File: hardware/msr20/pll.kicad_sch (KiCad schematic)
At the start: 9 parts, among them U6 74LS163, U7 CD74HC4046

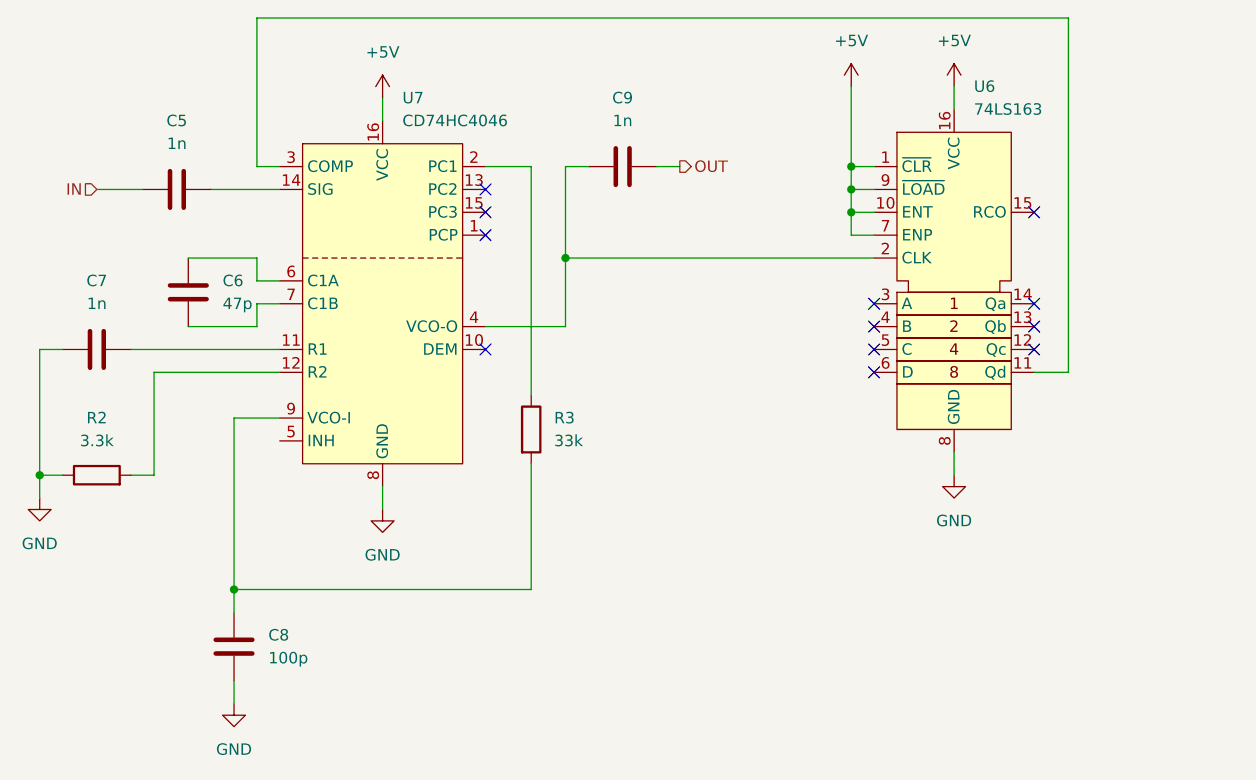
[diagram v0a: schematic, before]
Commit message: add test points to schematic
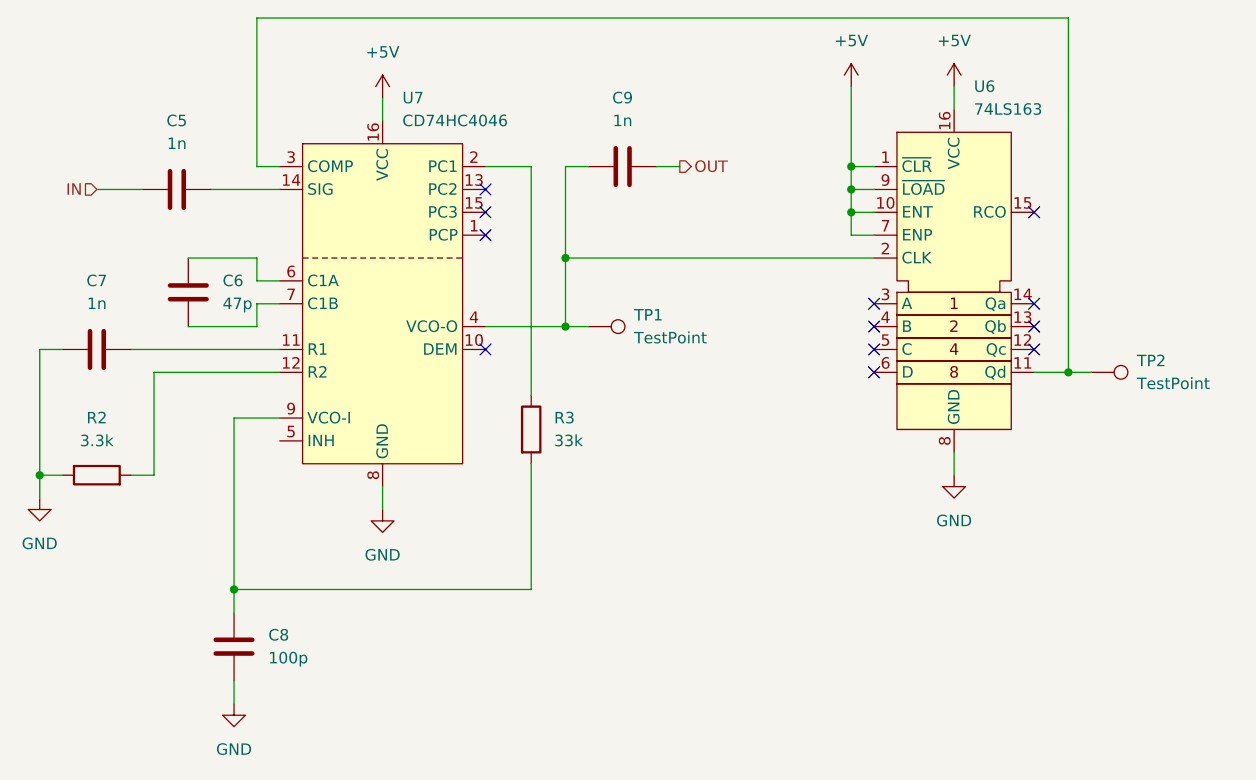
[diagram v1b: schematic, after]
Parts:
- added TP1, TP2: TestPoint, TestPoint:TestPoint_Pad_D1.0mm, symbol Connector:TestPoint
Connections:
- net at U6.11 (Qd), U7.3 (COMP): now also TP2.1
- net at C9.1, U6.2 (CLK), U7.4 (VCO-O): now also TP1.1
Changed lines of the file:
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@@
+		(color 0 0 0 0)
+	)
+	(junction
+		(at 121.92 93.98)
+		(diameter 0)
+		(color 0 0 0 0)
+	)
+	(junction
+		(at 177.8 99.06)
+		(diameter 0)
 		(color 0 0 0 0)
 	)
@@
 	(wire
 		(pts
+			(xy 121.92 93.98) (xy 124.46 93.98)
+		)
+		(stroke
+			(width 0)
+			(type default)
+		)
+	)
+	(wire
+		(pts
 			(xy 121.92 86.36) (xy 156.21 86.36)
 		)
@@
 		(pts
 			(xy 85.09 123.19) (xy 85.09 125.73)
+		)
+		(stroke
+			(width 0)
+			(type default)
+		)
+	)
+	(wire
+		(pts
+			(xy 177.8 99.06) (xy 180.34 99.06)
 		)
 		(stroke
@@
 	)
 	(symbol
+		(lib_id "Connector:TestPoint")
+		(at 180.34 99.06 270)
+		(unit 1)
+		(exclude_from_sim no)
+		(in_bom yes)
+		(on_board yes)
+		(dnp no)
+		(fields_autoplaced yes)
+		(property "Reference" "TP2"
+			(at 185.42 97.7899 90)
+			(effects
+				(font
+					(size 1.27 1.27)
+				)
+				(justify left)
+			)
+		)
+		(property "Value" "TestPoint"
+			(at 185.42 100.3299 90)
+			(effects
+				(font
+					(size 1.27 1.27)
+				)
+				(justify left)
+			)
+		)
+		(property "Footprint" "TestPoint:TestPoint_Pad_D1.0mm"
+			(at 180.34 104.14 0)
+			(effects
+				(font
+					(size 1.27 1.27)
+				)
+				(hide yes)
+			)
+		)
+		(property "Datasheet" "~"
+			(at 180.34 104.14 0)
+			(effects
+				(font
+					(size 1.27 1.27)
+				)
+				(hide yes)
+			)
+		)
+		(property "Description" "test point"
+			(at 180.34 99.06 0)
+			(effects
+				(font
+					(size 1.27 1.27)
+				)
+				(hide yes)
+			)
+		)
+		(pin "1"
+		)
+		(instances
+			(project "msr20"
+				(path "/827e4c90-6b76-4aba-b6da-8b66ea005818/879e4ab0-ee5d-4d03-b0f3-e28ce814003c"
+					(reference "TP2")
+					(unit 1)
+				)
+			)
+		)
+	)
+	(symbol
 		(lib_id "power:GND")
 		(at 101.6 114.3 0)
@@
 					(unit 1)
 				)
+			)
+		)
+	)
+	(symbol
+		(lib_id "Connector:TestPoint")
+		(at 124.46 93.98 270)
+		(unit 1)
+		(exclude_from_sim no)
+		(in_bom yes)
+		(on_board yes)
+		(dnp no)
+		(fields_autoplaced yes)
+		(property "Reference" "TP1"
+			(at 129.54 92.7099 90)
+			(effects
+				(font
+					(size 1.27 1.27)
+				)
+				(justify left)
+			)
+		)
+		(property "Value" "TestPoint"
+			(at 129.54 95.2499 90)
+			(effects
+				(font
+					(size 1.27 1.27)
+				)
+				(justify left)
+			)
+		)
+		(property "Footprint" "TestPoint:TestPoint_Pad_D1.0mm"
+			(at 124.46 99.06 0)
+			(effects
+				(font
+					(size 1.27 1.27)
+				)
+				(hide yes)
+			)
+		)
+		(property "Datasheet" "~"
+			(at 124.46 99.06 0)
+			(effects
+				(font
+					(size 1.27 1.27)
+				)
+				(hide yes)
+			)
+		)
+		(property "Description" "test point"
+			(at 124.46 93.98 0)
+			(effects
+				(font
+					(size 1.27 1.27)
+				)
+				(hide yes)
+			)
+		)
+		(pin "1"
+		)
+		(instances
+			(project "msr20"
+				(path "/827e4c90-6b76-4aba-b6da-8b66ea005818/879e4ab0-ee5d-4d03-b0f3-e28ce814003c"
+					(reference "TP1")
+					(unit 1)
+				)
